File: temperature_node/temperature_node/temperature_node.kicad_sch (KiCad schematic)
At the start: 33 parts, among them CN1 UART, J1 USB_C_Receptacle_USB2.0_16P, J2 S2B-PH-K-S, U1 SHT40-AD1B-R3, U2 MCP73831-2-OT, U3 MIC5504-3.3YM5, U4 ESP32-C3-WROOM-02

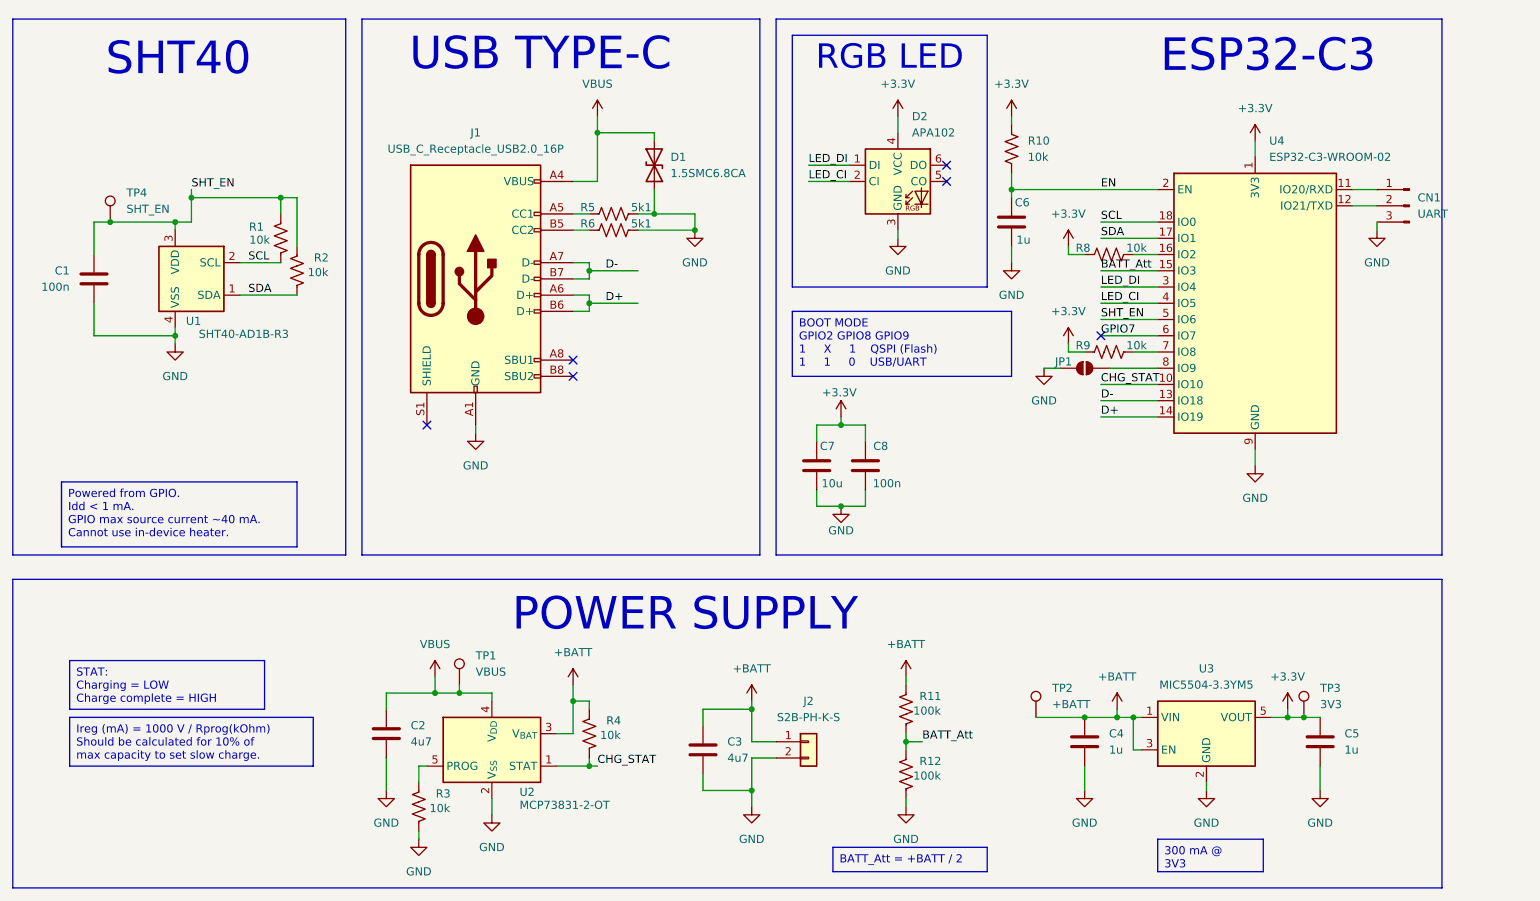
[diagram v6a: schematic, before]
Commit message: Add GND test point and rearrange some nodes
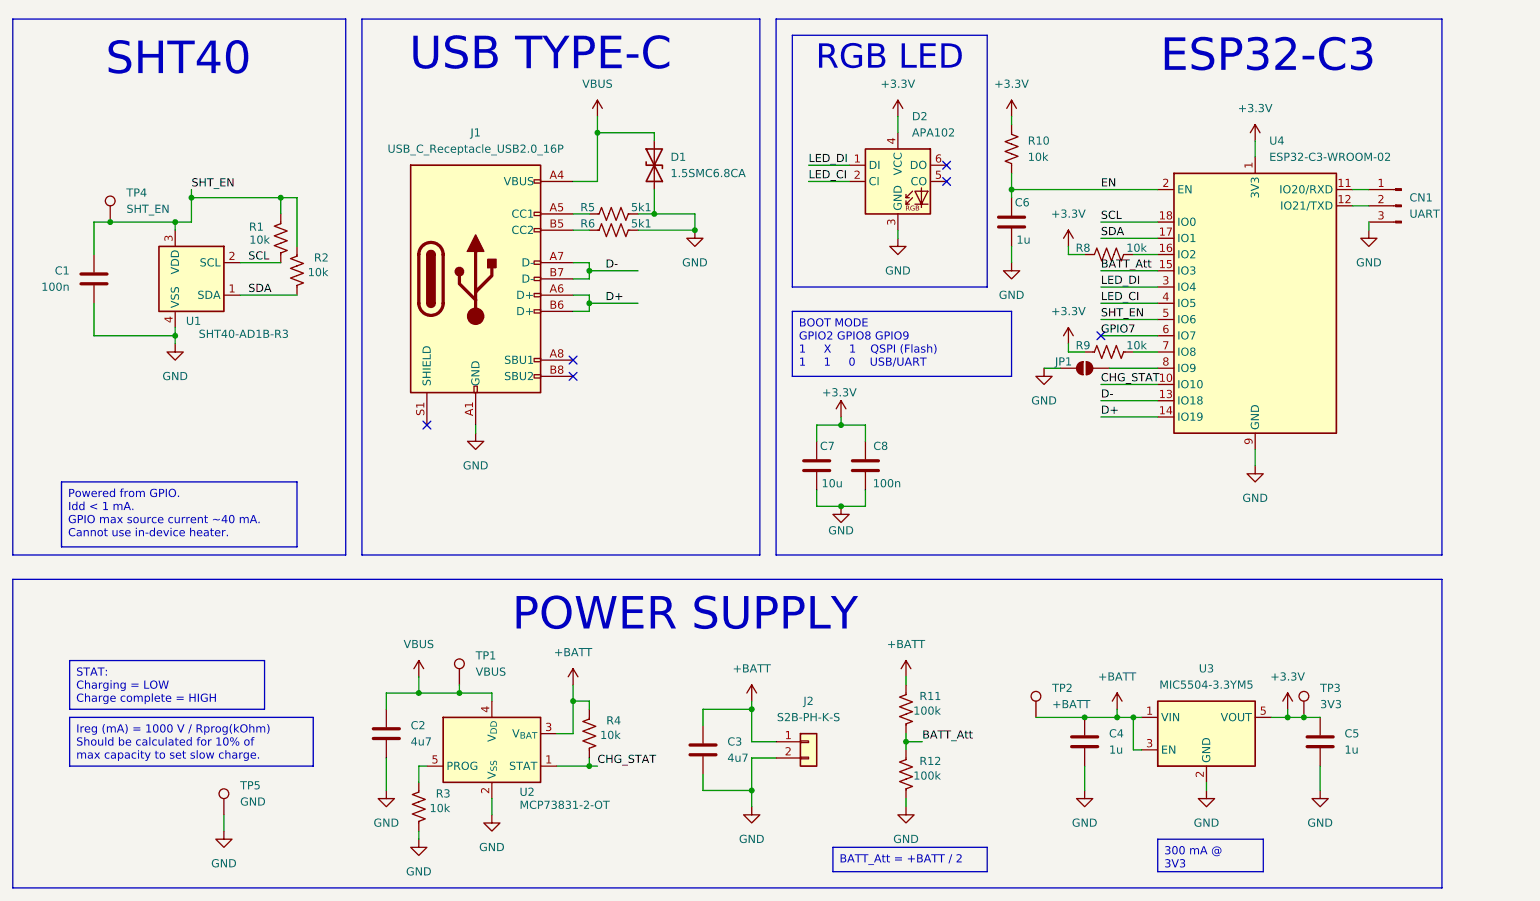
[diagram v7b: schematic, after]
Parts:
- added TP5: GND, TestPoint:TestPoint_Pad_D1.0mm, symbol Connector:TestPoint
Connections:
- net GND: now also TP5.1
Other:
- moved on the sheet: CN1
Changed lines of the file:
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@@
 	(paper "A4")
 	(junction
-		(at 101.6 129.54)
-		(diameter 0)
-		(color 0 0 0 0)
-	)
-	(junction
 		(at 208.28 133.35)
 		(diameter 0)
@@
 	)
 	(junction
+		(at 99.06 129.54)
+		(diameter 0)
+		(color 0 0 0 0)
+	)
+	(junction
 		(at 125.73 140.97)
 		(diameter 0)
@@
 	(wire
 		(pts
+			(xy 99.06 129.54) (xy 105.41 129.54)
+		)
+		(stroke
+			(width 0)
+			(type default)
+		)
+	)
+	(wire
+		(pts
 			(xy 175.26 137.16) (xy 175.26 138.43)
 		)
@@
 	(wire
 		(pts
+			(xy 99.06 129.54) (xy 93.98 129.54)
+		)
+		(stroke
+			(width 0)
+			(type default)
+		)
+	)
+	(wire
+		(pts
 			(xy 63.5 55.88) (xy 60.96 55.88)
 		)
@@
 	(wire
 		(pts
+			(xy 68.58 148.59) (xy 68.58 151.13)
+		)
+		(stroke
+			(width 0)
+			(type default)
+		)
+	)
+	(wire
+		(pts
 			(xy 127 49.53) (xy 123.19 49.53)
 		)
@@
 	(wire
 		(pts
-			(xy 101.6 129.54) (xy 93.98 129.54)
-		)
-		(stroke
-			(width 0)
-			(type default)
-		)
-	)
-	(wire
-		(pts
 			(xy 125.73 140.97) (xy 125.73 139.7)
 		)
@@
 	(wire
 		(pts
-			(xy 101.6 127) (xy 101.6 129.54)
+			(xy 99.06 127) (xy 99.06 129.54)
 		)
 		(stroke
@@
 	(wire
 		(pts
-			(xy 248.92 50.8) (xy 245.11 50.8)
+			(xy 247.65 50.8) (xy 245.11 50.8)
 		)
 		(stroke
@@
 	(wire
 		(pts
-			(xy 248.92 53.34) (xy 245.11 53.34)
+			(xy 247.65 53.34) (xy 245.11 53.34)
 		)
 		(stroke
@@
 	(wire
 		(pts
-			(xy 101.6 129.54) (xy 105.41 129.54)
-		)
-		(stroke
-			(width 0)
-			(type default)
-		)
-	)
-	(wire
-		(pts
-			(xy 248.92 55.88) (xy 248.92 57.15)
+			(xy 247.65 55.88) (xy 247.65 57.15)
 		)
 		(stroke
@@
 	(symbol
 		(lib_id "Connector:Conn_01x03_Pin")
-		(at 254 53.34 0)
+		(at 252.73 53.34 0)
 		(mirror y)
 		(unit 1)
@@
 		(fields_autoplaced yes)
 		(property "Reference" "CN1"
-			(at 255.27 52.0699 0)
+			(at 254 52.0699 0)
 			(effects
 				(font
@@
 		)
 		(property "Value" "UART"
-			(at 255.27 54.6099 0)
+			(at 254 54.6099 0)
 			(effects
 				(font
@@
 		)
 		(property "Footprint" "Connector_Wire:SolderWire-0.1sqmm_1x03_P3.6mm_D0.4mm_OD1mm"
-			(at 254 53.34 0)
+			(at 252.73 53.34 0)
 			(effects
 				(font
@@
 		)
 		(property "Datasheet" "~"
-			(at 254 53.34 0)
+			(at 252.73 53.34 0)
 			(effects
 				(font
@@
 		)
 		(property "Description" "Generic connector, single row, 01x03, script generated"
-			(at 254 53.34 0)
+			(at 252.73 53.34 0)
 			(effects
 				(font
@@
 	(symbol
 		(lib_id "power:GND")
-		(at 248.92 57.15 0)
+		(at 247.65 57.15 0)
 		(unit 1)
 		(exclude_from_sim no)
@@
 		(fields_autoplaced yes)
 		(property "Reference" "#PWR025"
-			(at 248.92 63.5 0)
+			(at 247.65 63.5 0)
 			(effects
 				(font
@@
 		)
 		(property "Value" "GND"
-			(at 248.92 62.23 0)
+			(at 247.65 62.23 0)
 			(effects
 				(font
@@
 		)
 		(property "Footprint" ""
-			(at 248.92 57.15 0)
+			(at 247.65 57.15 0)
 			(effects
 				(font
@@
 		)
 		(property "Datasheet" ""
-			(at 248.92 57.15 0)
+			(at 247.65 57.15 0)
 			(effects
 				(font
@@
 		)
 		(property "Description" "Power symbol creates a global label with name \"GND\" , ground"
-			(at 248.92 57.15 0)
+			(at 247.65 57.15 0)
 			(effects
 				(font
@@
 	)
 	(symbol
+		(lib_id "Connector:TestPoint")
+		(at 68.58 148.59 0)
+		(unit 1)
+		(exclude_from_sim no)
+		(in_bom yes)
+		(on_board yes)
+		(dnp no)
+		(fields_autoplaced yes)
+		(property "Reference" "TP5"
+			(at 71.12 144.0179 0)
+			(effects
+				(font
+					(size 1.27 1.27)
+				)
+				(justify left)
+			)
+		)
+		(property "Value" "GND"
+			(at 71.12 146.5579 0)
+			(effects
+				(font
+					(size 1.27 1.27)
+				)
+				(justify left)
+			)
+		)
+		(property "Footprint" "TestPoint:TestPoint_Pad_D1.0mm"
+			(at 73.66 148.59 0)
+			(effects
+				(font
+					(size 1.27 1.27)
+				)
+				(hide yes)
+			)
+		)
+		(property "Datasheet" "~"
+			(at 73.66 148.59 0)
+			(effects
+				(font
+					(size 1.27 1.27)
+				)
+				(hide yes)
+			)
+		)
+		(property "Description" "test point"
+			(at 68.58 148.59 0)
+			(effects
+				(font
+					(size 1.27 1.27)
+				)
+				(hide yes)
+			)
+		)
+		(pin "1"
+		)
+		(instances
+			(project "temperature_node"
+				(path "/b4f604dd-c1be-4776-9f83-5b1c508883b1"
+					(reference "TP5")
+					(unit 1)
+				)
+			)
+		)
+	)
+	(symbol
 		(lib_id "power:+3.3V")
 		(at 191.77 39.37 0)
@@
 	)
 	(symbol
+		(lib_id "power:GND")
+		(at 68.58 151.13 0)
+		(unit 1)
+		(exclude_from_sim no)
+		(in_bom yes)
+		(on_board yes)
+		(dnp no)
+		(fields_autoplaced yes)
+		(property "Reference" "#PWR031"
+			(at 68.58 157.48 0)
+			(effects
+				(font
+					(size 1.27 1.27)
+				)
+				(hide yes)
+			)
+		)
+		(property "Value" "GND"
+			(at 68.58 156.21 0)
+			(effects
+				(font
+					(size 1.27 1.27)
+				)
+			)
+		)
+		(property "Footprint" ""
+			(at 68.58 151.13 0)
+			(effects
+				(font
+					(size 1.27 1.27)
+				)
+				(hide yes)
+			)
+		)
+		(property "Datasheet" ""
+			(at 68.58 151.13 0)
+			(effects
+				(font
+					(size 1.27 1.27)
+				)
+				(hide yes)
+			)
+		)
+		(property "Description" "Power symbol creates a global label with name \"GND\" , ground"
+			(at 68.58 151.13 0)
+			(effects
+				(font
+					(size 1.27 1.27)
+				)
+				(hide yes)
+			)
+		)
+		(pin "1"
+		)
+		(instances
+			(project "temperature_node"
+				(path "/b4f604dd-c1be-4776-9f83-5b1c508883b1"
+					(reference "#PWR031")
+					(unit 1)
+				)
+			)
+		)
+	)
+	(symbol
 		(lib_id "Device:R_US")
 		(at 80.01 63.5 0)
@@
 	(symbol
 		(lib_id "power:VBUS")
-		(at 101.6 127 0)
+		(at 99.06 127 0)
 		(unit 1)
 		(exclude_from_sim no)
@@
 		(fields_autoplaced yes)
 		(property "Reference" "#PWR02"
-			(at 101.6 130.81 0)
+			(at 99.06 130.81 0)
 			(effects
 				(font
@@
 		)
 		(property "Value" "VBUS"
-			(at 101.6 121.92 0)
+			(at 99.06 121.92 0)
 			(effects
 				(font
@@
 		)
 		(property "Footprint" ""
-			(at 101.6 127 0)
+			(at 99.06 127 0)
 			(effects
 				(font
@@
 		)
 		(property "Datasheet" ""
-			(at 101.6 127 0)
+			(at 99.06 127 0)
 			(effects
 				(font
@@
 		)
 		(property "Description" "Power symbol creates a global label with name \"VBUS\""
-			(at 101.6 127 0)
+			(at 99.06 127 0)
 			(effects
 				(font

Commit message: Change battery connector to SMD
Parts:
- J2: footprint Connector_JST:JST_PH_S2B-PH-K_1x02_P2.00mm_Horizontal -> Connector_JST:JST_PH_S2B-PH-SM4-TB_1x02-1MP_P2.00mm_Horizontal
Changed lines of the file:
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@@
 			)
 		)
-		(property "Footprint" "Connector_JST:JST_PH_S2B-PH-K_1x02_P2.00mm_Horizontal"
+		(property "Footprint" "Connector_JST:JST_PH_S2B-PH-SM4-TB_1x02-1MP_P2.00mm_Horizontal"
 			(at 160.02 137.16 0)
 			(effects
